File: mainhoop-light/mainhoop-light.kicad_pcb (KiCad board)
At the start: 2 copper layers, 74 x 69 mm, 79 parts, among them IC1 BCR420U, IC3 BCR420U, IC4 BCR420U, IC5 BCR420U, IC6 BCR420U, J1 Conn_01x04, Q1 2N7002, Q10 Si2301CDS, Q11 2N7002, Q2 Si2301CDS, Q3 2N7002, Q4 2N7002, Q5 Si2301CDS, Q6 2N7002, Q8 2N7002, Q9 2N7002, U1 AP2204K-ADJ, U2 SE555D

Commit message: Add files via upload
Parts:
- removed Q10, Q5: Si2301CDS, Package_TO_SOT_SMD:SOT-23
- removed Q11, Q4, Q6, Q8, Q9: 2N7002, Package_TO_SOT_SMD:SOT-23
- removed R15, R16, R17: 1M, Resistor_SMD:R_0603_1608Metric
- removed R18, R19: 100k, Resistor_SMD:R_0603_1608Metric
- removed kibuzzard-67907CEC (x2): G***, kibuzzard-67907CEC
- added Q12: Si2301CDS, Package_TO_SOT_SMD:SOT-23, F.Cu at (68.0, 32.9)
- added Q13: 2N7002, Package_TO_SOT_SMD:SOT-23, F.Cu at (105.0, 75.0)
- added Q14: 2N7002, Package_TO_SOT_SMD:SOT-23, F.Cu at (90.1, 71.5)
- added Q15: Si2301CDS, Package_TO_SOT_SMD:SOT-23, F.Cu at (105.0, 70.5)
- added Q16: 2N7002, Package_TO_SOT_SMD:SOT-23, F.Cu at (99.5, 74.0)
- added Q7: 2N7002, Package_TO_SOT_SMD:SOT-23, F.Cu at (69.5, 27.4)
- added R22: 10k, Resistor_SMD:R_0603_1608Metric, F.Cu at (64.5, 33.1)
- added R23: 10k, Resistor_SMD:R_0603_1608Metric, F.Cu at (109.0, 70.8)
- added R24: 10k, Resistor_SMD:R_0603_1608Metric, F.Cu at (101.0, 69.8)
- Q2: value Si2301CDS -> 2N7002
- Q3: value 2N7002 -> Si2301CDS
- R1, R6: value 100k -> 10k
- R11, R12, R13: value 1M -> 10k
- moved G*** 79.8 mm to (129.0, 34.5)
- moved R11 47.4 mm to (72.0, 32.3), turned to -90 degrees
- moved R4 45.5 mm to (68.1, 74.2)
- moved IC6 40.0 mm to (102.0, 26.4)
- moved R7 39.8 mm to (106.1, 26.3)
- moved R10 39.0 mm to (96.6, 26.3)
- moved IC3 38.7 mm to (92.8, 26.4)
- moved R14 36.5 mm to (125.2, 61.0), turned to 180 degrees
- moved R3 35.7 mm to (133.1, 65.8), turned to -90 degrees
- moved IC1 34.5 mm to (120.3, 61.5)
- moved C2 33.9 mm to (129.4, 62.0), turned to 180 degrees
- moved G*** 31.5 mm to (111.0, 61.0)
- moved R5 31.1 mm to (68.1, 61.8), turned to 0 degrees
- moved R13 30.9 mm to (96.8, 70.5), turned to 0 degrees
- moved R8 30.0 mm to (106.1, 31.3)
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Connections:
- net TSAL renamed RTML
- IC1 pad 1: TSAL_EN -> RTML_EN
- Q1 pad 1: Net-(Q1-G) -> TSSI
- Q1 pad 2: Net-(Q1-S) -> GND
- Q2 pad 1: TSSI -> Net-(Q1-D)
- Q2 pad 2: +12V -> Net-(Q13-S)
- Q2 pad 3: GREEN_EN -> Net-(Q2-D)
- Q3 pad 1: TSSI -> Net-(Q2-D)
- Q3 pad 2: GND -> +12V
- Q3 pad 3: Net-(Q1-G) -> RED_EN
- R1 pad 1: +12V -> Net-(Q1-D)
- R1 pad 2: Net-(Q1-D) -> +12V
- R11 pad 1: Net-(R11-Pad1) -> GND
- R11 pad 2: Net-(Q4-G) -> GREEN_EN
- R12 pad 2: Net-(Q4-G) -> RED_EN
- R13 pad 1: Net-(U2-Q) -> GND
- R13 pad 2: Net-(R11-Pad1) -> RTML_EN
- R4 pad 1: GND -> +5V
- R6 pad 1: +12V -> Net-(Q2-D)
- R6 pad 2: Net-(Q1-G) -> +12V
- U2 pad 3: Net-(U2-Q) -> Net-(Q14-G)
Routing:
- net GND: track 23.2 -> 235.8 mm, vias 336 -> 4
- net TSAL_EN: track 40.6 -> 0.00 mm, vias 2 -> 0
- net Net-(Q9-G): track 40.2 -> 0.00 mm, vias 2 -> 0
- net TSSI: track 36.1 -> 75.5 mm, vias 0 -> 3
- net +12V: track 93.6 -> 122.2 mm, vias 5 -> 4
- net RTML_EN: track 0.00 -> 28.4 mm
- net Net-(Q4-G): track 27.7 -> 0.00 mm, vias 2 -> 0
- net Net-(D14-BK): track 68.6 -> 42.9 mm
- net Net-(Q14-G): track 0.00 -> 23.3 mm, vias 0 -> 2
- net Net-(D7-BK): track 50.1 -> 27.0 mm
- net THR: track 14.6 -> 36.4 mm
- net Net-(Q13-S): track 0.00 -> 21.6 mm, vias 0 -> 2
- net Net-(U2-Q): track 15.4 -> 0.00 mm
- net Net-(IC1-OUT_1): track 36.7 -> 48.8 mm
- net Net-(Q10-G): track 10.7 -> 0.00 mm
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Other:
- board size 74 x 69 mm -> 74 x 57 mm
- board text added: "NCKU Formula Racing RTML & TSSI Rev. 2026.04"
- board text removed: "-"
- board text removed: "NCKU Formula Racing RTML & TSSI Rev. 2025.02"
- board text removed: "R=6.0"
- board text removed: "R=7.0"

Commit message: Add files via upload
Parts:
- moved G*** 2.06 mm to (109.0, 60.5)
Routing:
- net GND: vias 4 -> 279

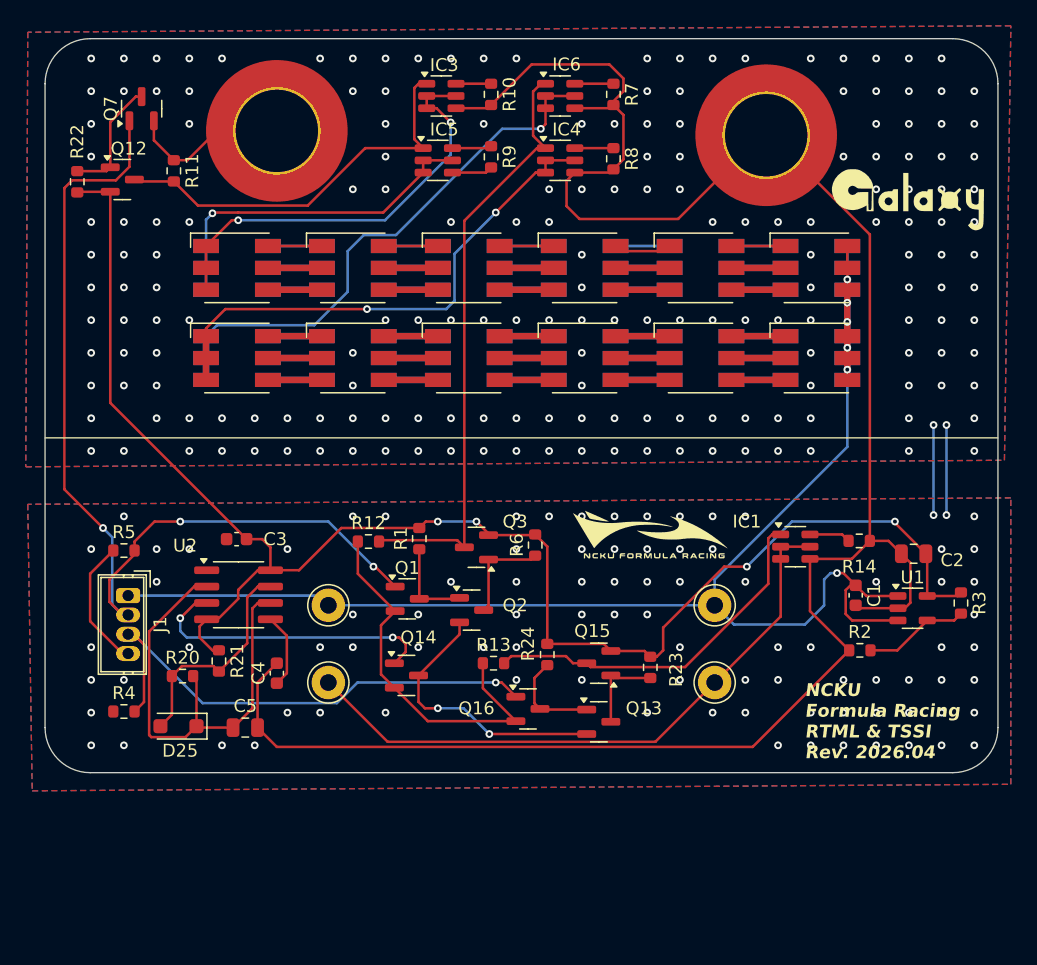
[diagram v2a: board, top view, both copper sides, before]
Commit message: finish mainhoop-light layout
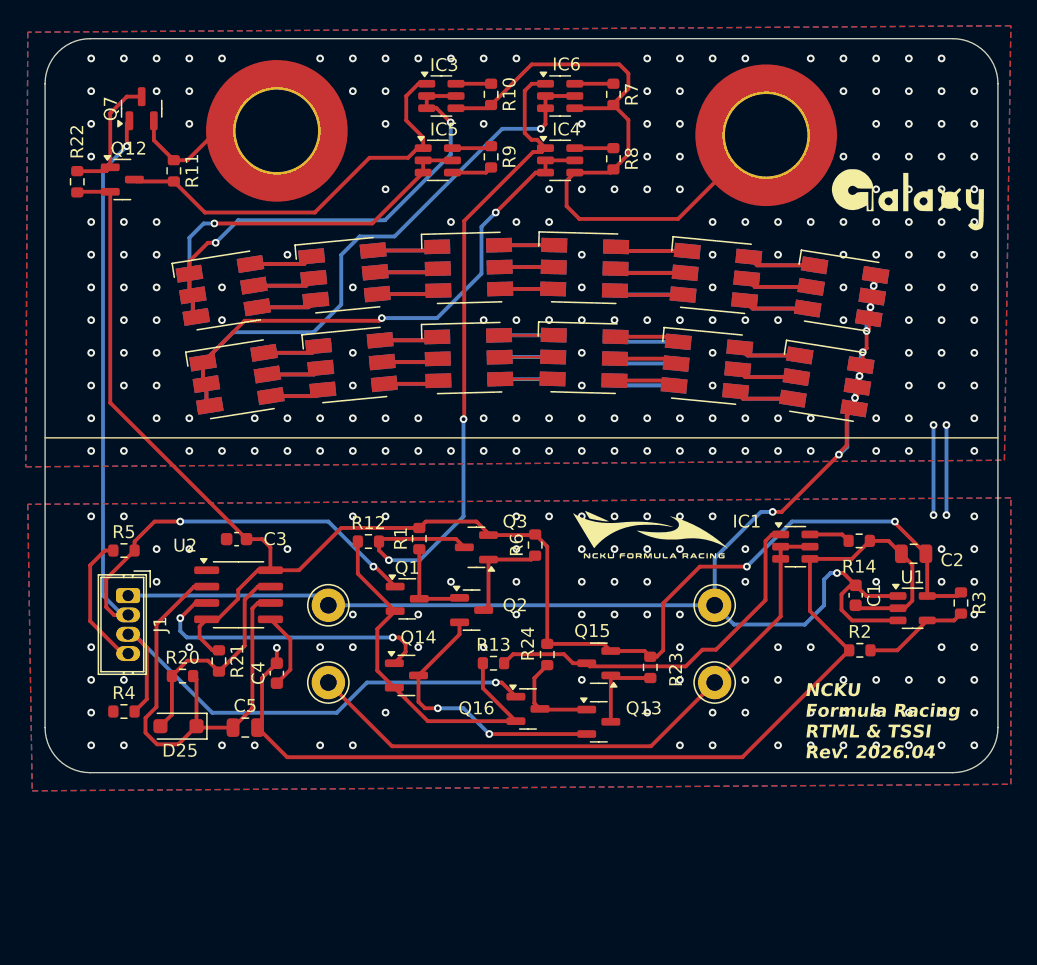
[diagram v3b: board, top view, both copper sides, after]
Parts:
- moved D12 2.70 mm to (123.9, 41.7), turned to -9 degrees
- moved D6 2.70 mm to (123.9, 41.7), turned to -9 degrees
- moved D1 2.05 mm to (75.8, 41.6), turned to 9 degrees
- moved D7 2.05 mm to (75.8, 41.6), turned to 9 degrees
- moved D23 2.02 mm to (122.7, 48.7), turned to -9 degrees
- moved D24 2.02 mm to (122.7, 48.7), turned to -9 degrees
- moved D14 1.65 mm to (76.9, 48.5), turned to 9 degrees
- moved D13 1.65 mm to (76.9, 48.5), turned to 9 degrees
- moved D11 1.35 mm to (114.1, 40.4), turned to -5.5 degrees
- moved D5 1.35 mm to (114.1, 40.4), turned to -5.5 degrees
- moved D2 0.87 mm to (85.2, 40.4), turned to 5.5 degrees
- moved D8 0.87 mm to (85.2, 40.4), turned to 5.5 degrees
- moved D21 0.83 mm to (113.4, 47.5), turned to -5.5 degrees
- moved D22 0.83 mm to (113.4, 47.5), turned to -5.5 degrees
- moved D16 0.56 mm to (85.8, 47.3), turned to 5.5 degrees
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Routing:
- net GND: track 235.8 -> 204.3 mm
- net RED_EN: track 46.9 -> 54.8 mm, vias 0 -> 2
- net VDC: track 111.6 -> 116.3 mm, vias 6 -> 9
- net TSSI: track 75.5 -> 71.7 mm
- net Net-(D1-BK): track 33.4 -> 36.3 mm
- net Net-(D7-BK): track 27.0 -> 29.8 mm
- net Net-(D14-BK): track 42.9 -> 44.6 mm
- net Net-(D10-BA): track 4.20 -> 5.66 mm
- net Net-(D4-GA): track 4.20 -> 5.56 mm
- net Net-(D10-GA): track 4.20 -> 5.54 mm
- net Net-(D4-BA): track 4.20 -> 5.44 mm
- net Net-(D10-RA): track 4.20 -> 5.42 mm
- net Net-(D5-RA): track 4.20 -> 5.38 mm
- net Net-(D11-BA): track 4.20 -> 5.38 mm
- net Net-(D4-RA): track 4.53 -> 5.66 mm
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
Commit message: fix distance between pad to led
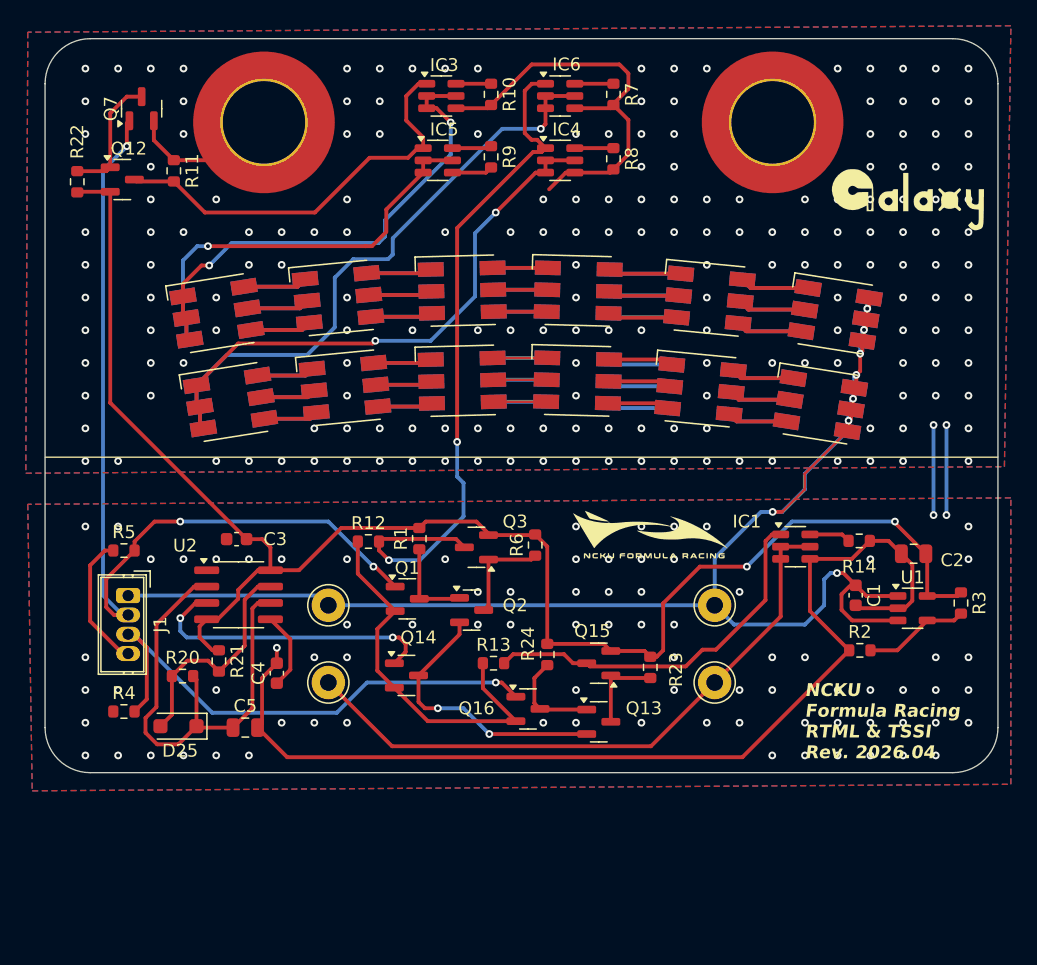
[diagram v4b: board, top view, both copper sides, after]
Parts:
- moved D1 1.83 mm to (75.3, 43.3)
- moved D10 1.83 mm to (103.4, 41.6)
- moved D11 1.83 mm to (113.6, 42.2)
- moved D12 1.83 mm to (123.4, 43.4)
- moved D13 1.83 mm to (76.4, 50.2)
- moved D14 1.83 mm to (76.4, 50.2)
- moved D15 1.83 mm to (85.3, 49.1)
- moved D16 1.83 mm to (85.3, 49.1)
- moved D17 1.83 mm to (94.4, 48.6)
- moved D18 1.83 mm to (94.4, 48.6)
- moved D19 1.83 mm to (103.4, 48.5)
- moved D2 1.83 mm to (84.7, 42.1)
- moved D20 1.83 mm to (103.4, 48.5)
- moved D21 1.83 mm to (112.9, 49.2)
- moved D22 1.83 mm to (112.9, 49.2)
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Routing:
- net GND: track 204.3 -> 189.2 mm, vias 279 -> 273
- net VDC: track 116.3 -> 119.2 mm, vias 9 -> 8
- net Net-(D7-BK): track 29.8 -> 32.1 mm
- net Net-(D14-BK): track 44.6 -> 46.5 mm
- net Net-(D13-BK): track 41.6 -> 43.6 mm
- net Net-(D1-BK): track 36.3 -> 38.3 mm

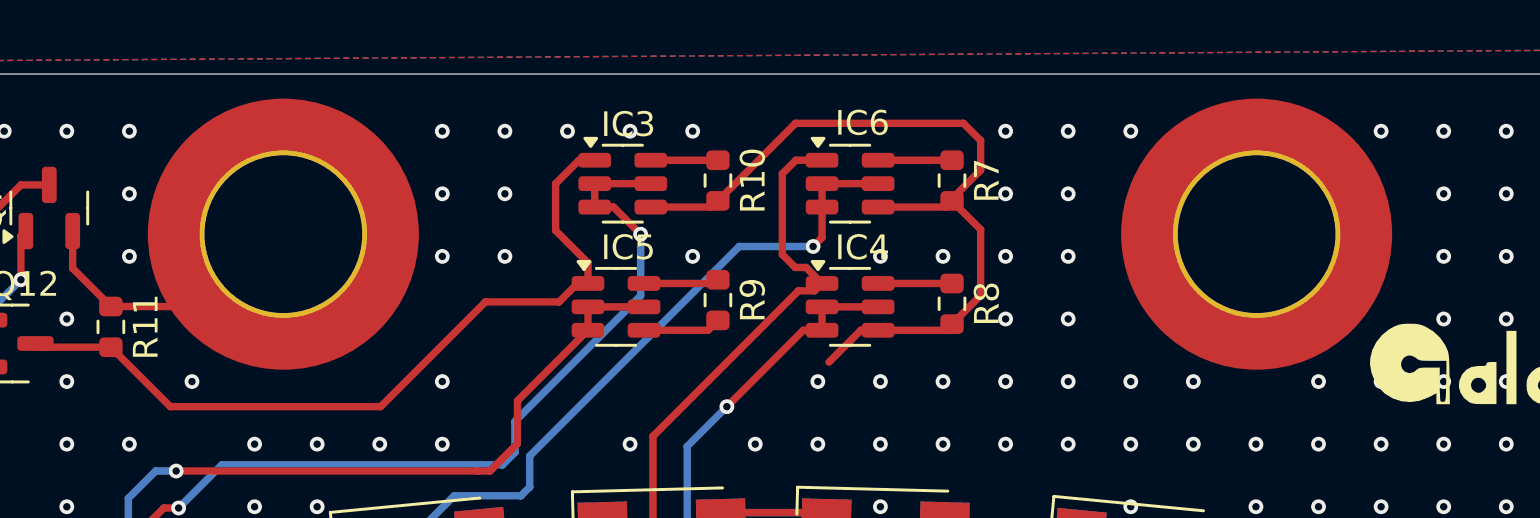
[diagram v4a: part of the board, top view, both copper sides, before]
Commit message: change the pads' size
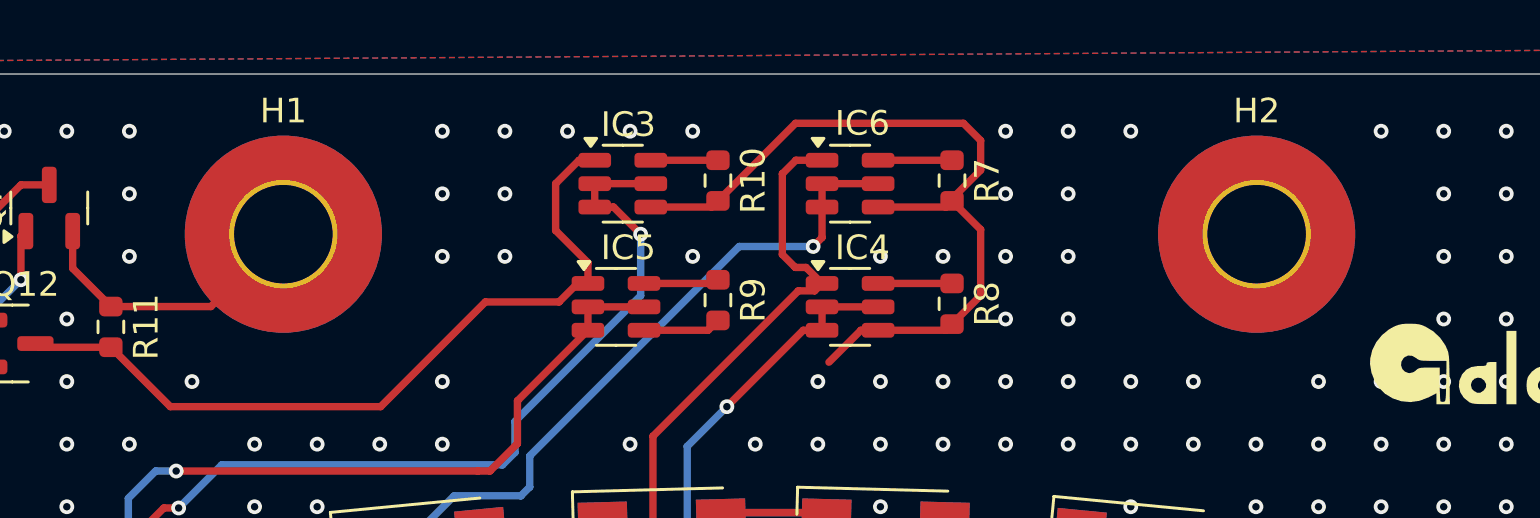
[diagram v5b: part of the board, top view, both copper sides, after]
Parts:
- H1, H2: footprint MountingHole:MountingHole_6.4mm_M6_DIN965_Pad_TopBottom -> MountingHole:MountingHole_4mm_Pad_TopBottom
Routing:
- net GND: track 189.2 -> 184.5 mm
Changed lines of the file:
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@@
     )
   )
-  (footprint "MountingHole:MountingHole_6.4mm_M6_DIN965_Pad_TopBottom" (layer "F.Cu")
+  (footprint "MountingHole:MountingHole_4mm_Pad_TopBottom" (layer "F.Cu")
     (at 118.5 28.5)
-    (descr "Mounting Hole 6.4mm, M6, DIN965")
-    (tags "mounting hole 6.4mm m6 din965")
+    (descr "Mounting Hole 4mm")
+    (tags "mounting hole 4mm")
     (property "Sheetfile" "mainhoop-light.kicad_sch")
     (property "Sheetname" "")
@@
     (property "ki_keywords" "mounting hole")
     (attr exclude_from_pos_files)
-    (fp_text reference "H2" (at 0 -6.5) (layer "F.SilkS") hide
-        (effects (font (size 1 1) (thickness 0.15)))
-    )
-    (fp_text value "M6_Pad" (at 0 6.5) (layer "F.Fab") hide
-        (effects (font (size 1 1) (thickness 0.15)))
-    )
-    (fp_text user "${REFERENCE}" (at 0 0) (layer "F.Fab") hide
-        (effects (font (size 1 1) (thickness 0.15)))
-    )
-    (fp_circle (center 0 0) (end 5.5 0)
+    (fp_text reference "H2" (at 0 -5) (layer "F.SilkS")
+        (effects (font (size 1 1) (thickness 0.15)))
+    )
+    (fp_text value "M6_Pad" (at 0 5) (layer "F.Fab")
+        (effects (font (size 1 1) (thickness 0.15)))
+    )
+    (fp_text user "${REFERENCE}" (at 0 0) (layer "F.Fab")
+        (effects (font (size 1 1) (thickness 0.15)))
+    )
+    (fp_circle (center 0 0) (end 4 0)
       (stroke (width 0.15) (type solid)) (fill none) (layer "Cmts.User"))
-    (fp_circle (center 0 0) (end 5.75 0)
+    (fp_circle (center 0 0) (end 4.25 0)
       (stroke (width 0.05) (type solid)) (fill none) (layer "F.CrtYd"))
-    (pad "" connect circle (at 0 0) (size 11 11) (layers "B.Mask" "Rescue"))
-    (pad "1" thru_hole circle (at 0 0) (size 6.8 6.8) (drill 6.4) (layers "*.Cu" "*.Mask")
+    (pad "1" thru_hole circle (at 0 0) (size 4.4 4.4) (drill 4) (layers "*.Cu" "*.Mask")
       (net 1 "GND") (pinfunction "1") (pintype "input"))
-    (pad "1" connect circle (at 0 0) (size 11 11) (layers "F.Cu" "F.Mask")
-      (net 1 "GND") (pinfunction "1") (pintype "input") (zone_connect 2))
+    (pad "1" connect circle (at 0 0) (size 8 8) (layers "F.Cu" "F.Mask")
+      (net 1 "GND") (pinfunction "1") (pintype "input"))
+    (pad "1" connect circle (at 0 0) (size 8 8) (layers "B.Cu" "B.Mask")
+      (net 1 "GND") (pinfunction "1") (pintype "input"))
   )
   (footprint "Resistor_SMD:R_0603_1608Metric" (layer "F.Cu")
@@
       (stroke (width 0) (type solid)) (fill solid) (layer "F.SilkS"))
   )
-  (footprint "MountingHole:MountingHole_6.4mm_M6_DIN965_Pad_TopBottom" (layer "F.Cu")
+  (footprint "MountingHole:MountingHole_4mm_Pad_TopBottom" (layer "F.Cu")
     (at 79 28.5)
-    (descr "Mounting Hole 6.4mm, M6, DIN965")
-    (tags "mounting hole 6.4mm m6 din965")
+    (descr "Mounting Hole 4mm")
+    (tags "mounting hole 4mm")
     (property "Sheetfile" "mainhoop-light.kicad_sch")
     (property "Sheetname" "")
@@
     (property "ki_keywords" "mounting hole")
     (attr exclude_from_pos_files)
-    (fp_text reference "H1" (at 0 -6.5) (layer "F.SilkS") hide
-        (effects (font (size 1 1) (thickness 0.15)))
-    )
-    (fp_text value "M6_Pad" (at 0 6.5) (layer "F.Fab") hide
-        (effects (font (size 1 1) (thickness 0.15)))
-    )
-    (fp_text user "${REFERENCE}" (at 0 0) (layer "F.Fab") hide
-        (effects (font (size 1 1) (thickness 0.15)))
-    )
-    (fp_circle (center 0 0) (end 5.5 0)
+    (fp_text reference "H1" (at 0 -5) (layer "F.SilkS")
+        (effects (font (size 1 1) (thickness 0.15)))
+    )
+    (fp_text value "M6_Pad" (at 0 5) (layer "F.Fab")
+        (effects (font (size 1 1) (thickness 0.15)))
+    )
+    (fp_text user "${REFERENCE}" (at 0 0) (layer "F.Fab")
+        (effects (font (size 1 1) (thickness 0.15)))
+    )
+    (fp_circle (center 0 0) (end 4 0)
       (stroke (width 0.15) (type solid)) (fill none) (layer "Cmts.User"))
-    (fp_circle (center 0 0) (end 5.75 0)
+    (fp_circle (center 0 0) (end 4.25 0)
       (stroke (width 0.05) (type solid)) (fill none) (layer "F.CrtYd"))
-    (pad "" connect circle (at 0 0) (size 11 11) (layers "B.Mask" "Rescue"))
-    (pad "1" thru_hole circle (at 0 0) (size 6.8 6.8) (drill 6.4) (layers "*.Cu" "*.Mask")
+    (pad "1" thru_hole circle (at 0 0) (size 4.4 4.4) (drill 4) (layers "*.Cu" "*.Mask")
       (net 1 "GND") (pinfunction "1") (pintype "input"))
-    (pad "1" connect circle (at 0 0) (size 11 11) (layers "F.Cu" "F.Mask")
-      (net 1 "GND") (pinfunction "1") (pintype "input") (zone_connect 2))
+    (pad "1" connect circle (at 0 0) (size 8 8) (layers "F.Cu" "F.Mask")
+      (net 1 "GND") (pinfunction "1") (pintype "input"))
+    (pad "1" connect circle (at 0 0) (size 8 8) (layers "B.Cu" "B.Mask")
+      (net 1 "GND") (pinfunction "1") (pintype "input"))
   )
   (footprint "Package_TO_SOT_SMD:SOT-23" (layer "F.Cu")
@@
   (segment (start 91.725 75) (end 89.125 72.4) (width 0.3) (layer "F.Cu") (net 1))
   (segment (start 106.1375 27.0625) (end 107.3 25.9) (width 0.3) (layer "F.Cu") (net 1))
-  (segment (start 80 29.16) (end 75.34 29.16) (width 0.3) (layer "F.Cu") (net 1))
   (segment (start 107.3 24.7) (end 106.6 24) (width 0.3) (layer "F.Cu") (net 1))
   (segment (start 106.6 24) (end 99.7875 24) (width 0.3) (layer "F.Cu") (net 1))
